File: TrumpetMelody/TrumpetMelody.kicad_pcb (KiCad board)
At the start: 2 copper layers, 76.2 x 68.6 mm, 79 parts, among them J1 USB_B_Micro, J2 Conn_01x05, J3 640456-3, J4 640456-3, SW1 SW_Push, U1 STM32F411RETx, U2 TLV62565DBVR, U3 MAX98357AETE_T, U4 MAX7375AXR805

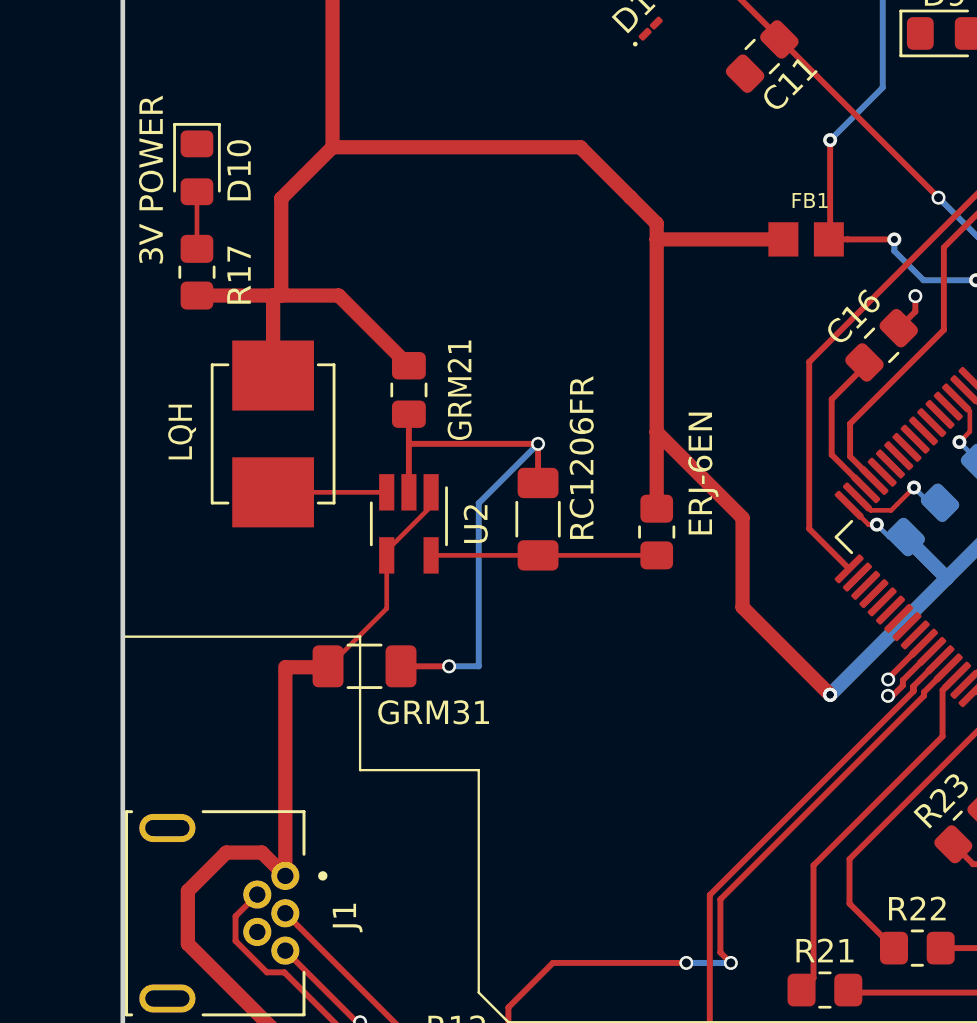
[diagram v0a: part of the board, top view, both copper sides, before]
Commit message: Manually added TI Webench PCB layout
I just sort of rotated the picture and drew it on
There's a bunch of holes in the PCB layout and I don't know if those are supposed to be vias or whatever. I may have used the wrong type of hole to switch board sides too.
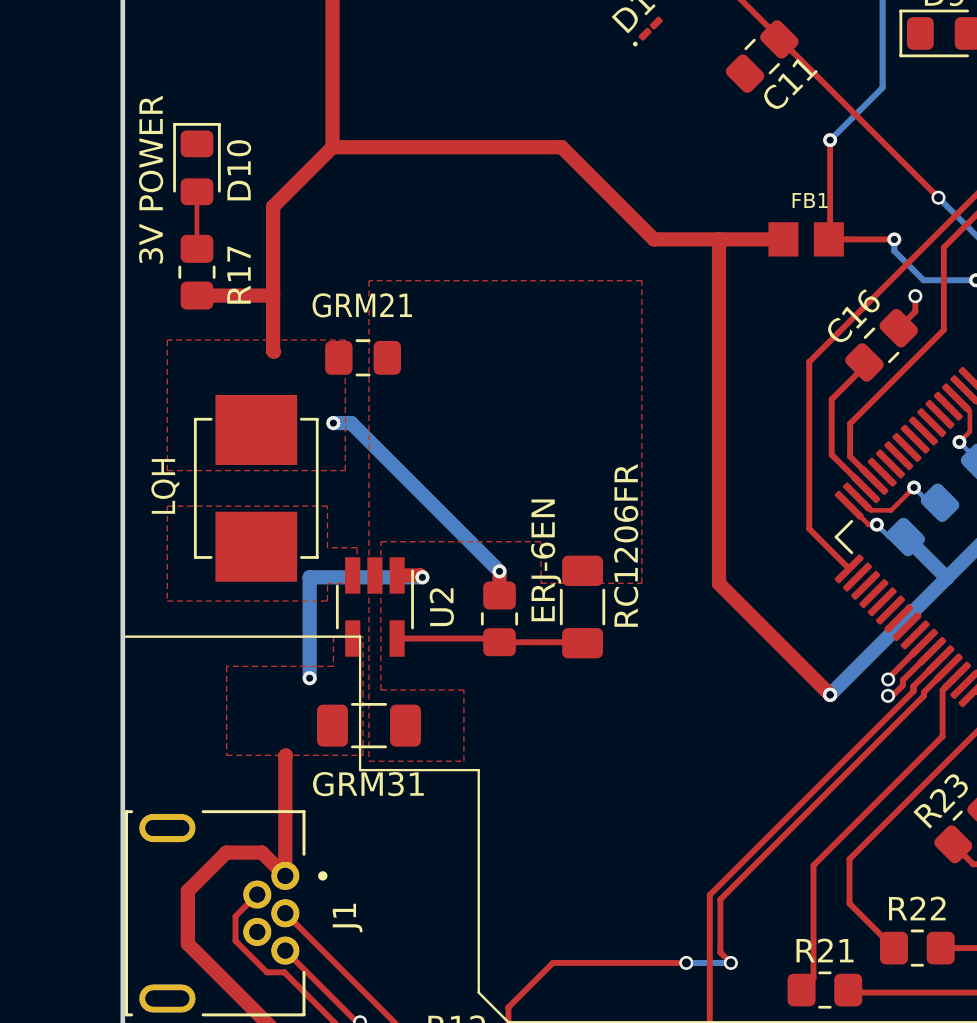
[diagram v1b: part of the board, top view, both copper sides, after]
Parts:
- moved ERJ-6EN 7.69 mm to (163.4, 86.9)
- moved RC1206FR 4.22 mm to (167.0, 86.4)
- moved U2 3.85 mm to (158.1, 86.4)
- moved GRM31 2.55 mm to (157.9, 91.4)
- moved LQH 2.44 mm to (153.0, 81.3)
- moved GRM21 2.40 mm to (157.6, 75.7), turned to 0 degrees
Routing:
- net GND: track 93.6 -> 69.2 mm, vias 15 -> 13
- net Net-(U2-SW): track 4.86 -> 0.00 mm
- net +5V: track 93.7 -> 89.0 mm, vias 0 -> 2
- net +3.3V: track 170.1 -> 168.2 mm, vias 9 -> 11
- net Net-(U2-FB): track 9.73 -> 8.02 mm
- added copper zone on F.Cu, net +3.3V
- added copper zone on F.Cu, net +5V
- added copper zone on F.Cu, net GND
- added copper zone on F.Cu, net Net-(U2-SW)

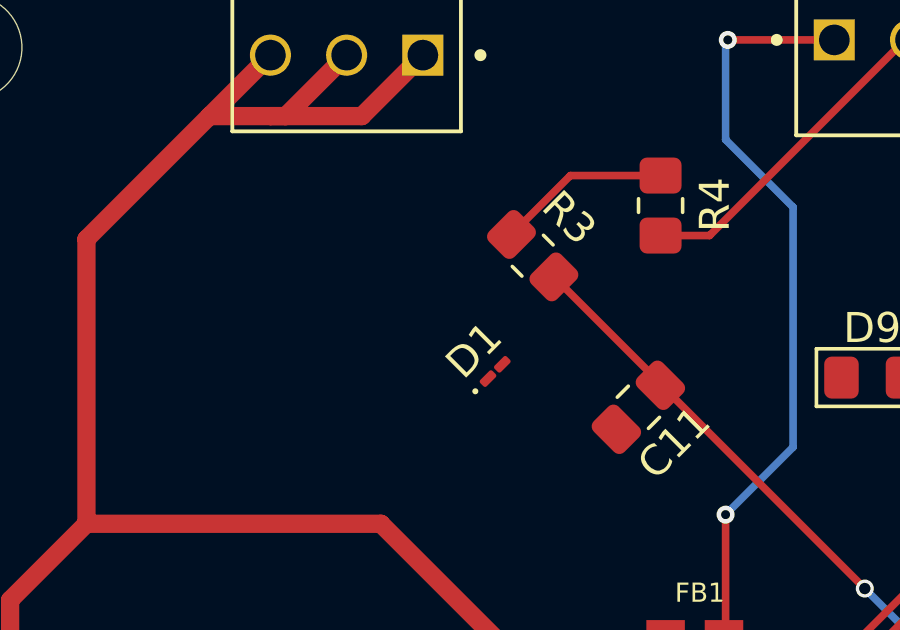
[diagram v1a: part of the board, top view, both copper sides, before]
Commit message: a diode on the linear pot got disconnected so i reconnected it
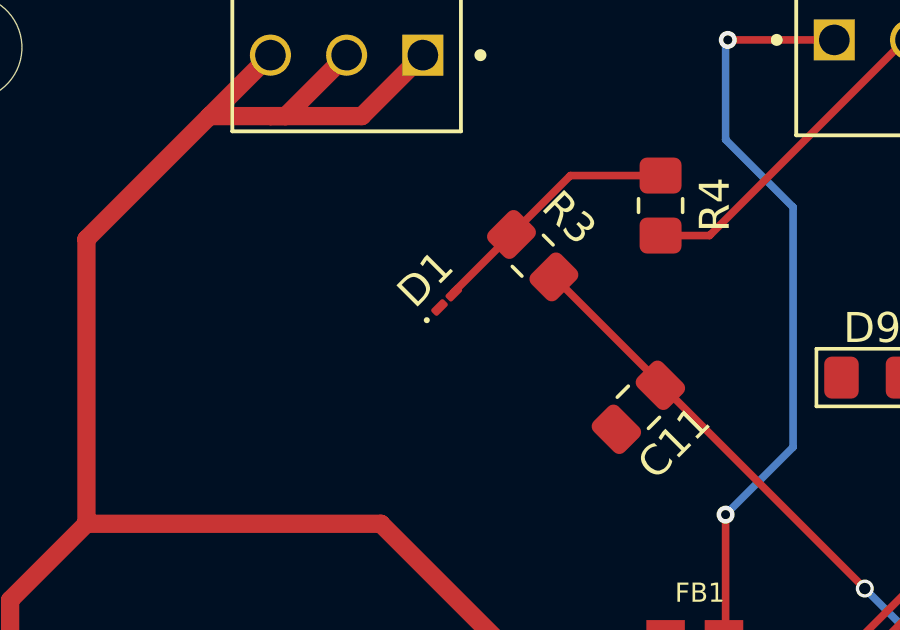
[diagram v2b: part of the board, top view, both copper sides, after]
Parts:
- moved D1 2.87 mm to (168.3, 59.2)
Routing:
- net Net-(D1-A2): track 5.78 -> 8.54 mm
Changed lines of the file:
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@@
   )
   (footprint "Diode_SMD:D_01005_0402Metric_Pad0.57x0.30mm_HandSolder" (layer "F.Cu")
-    (at 169.923674 61.597326 45)
+    (at 168.306325 59.227222 45)
     (descr "Diode SMD 01005 (0402 Metric), square (rectangular) end terminal, IPC_7351 nominal, (Body size source: http://www.vishay.com/docs/20056/crcw01005e3.pdf), generated with kicad-footprint-generator")
     (tags "diode handsolder")
@@
   (segment (start 194.937948 87.622948) (end 195.565896 86.995) (width 0.254) (layer "B.Cu") (net 13))
   (segment (start 210.185 69.85) (end 210.185 73.66) (width 0.254) (layer "B.Cu") (net 13))
+  (segment (start 168.544974 58.953798) (end 168.544974 58.988573) (width 0.254) (layer "F.Cu") (net 14))
   (segment (start 172.431572 55.0672) (end 175.4378 55.0672) (width 0.254) (layer "F.Cu") (net 14))
+  (segment (start 170.467586 57.031186) (end 168.544974 58.953798) (width 0.254) (layer "F.Cu") (net 14))
   (segment (start 170.467586 57.031186) (end 172.431572 55.0672) (width 0.254) (layer "F.Cu") (net 14))
   (segment (start 172.906777 98.880275) (end 172.906777 101.151777) (width 0.254) (layer "F.Cu") (net 15))

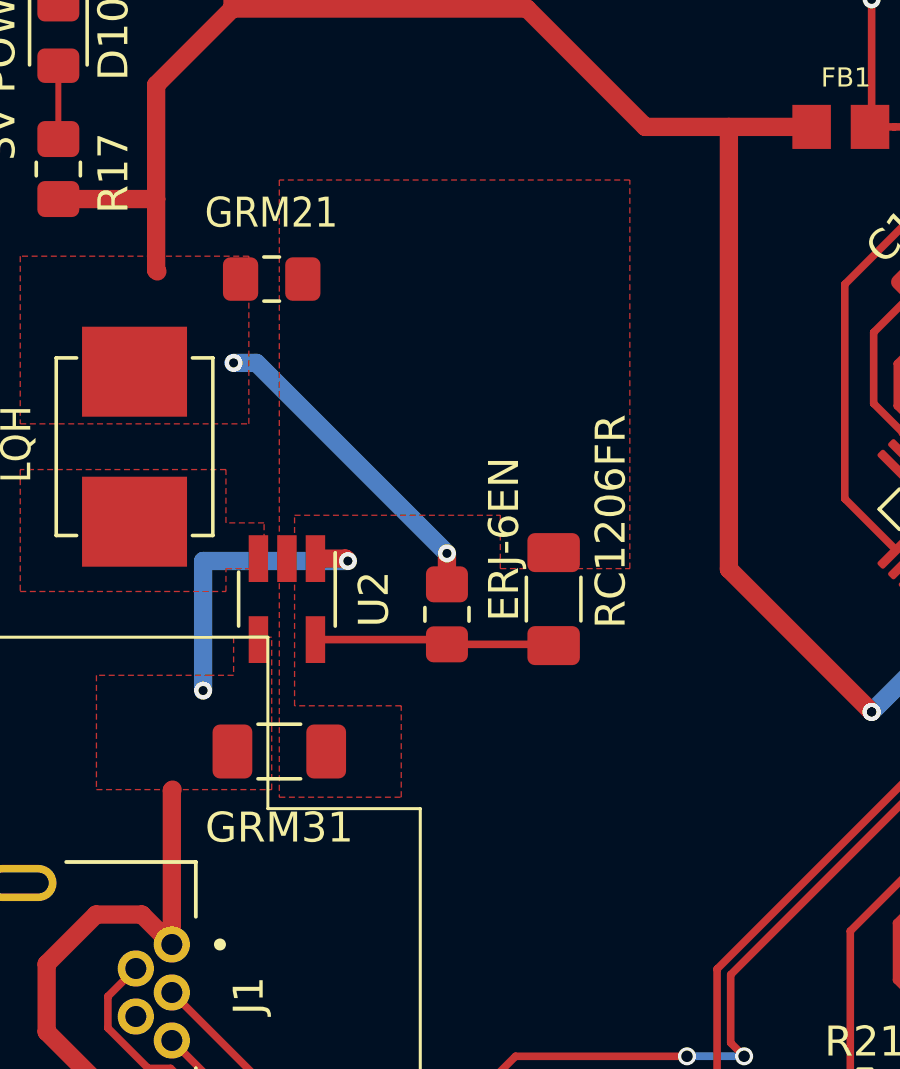
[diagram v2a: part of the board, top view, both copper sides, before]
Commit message: Added stitching vias
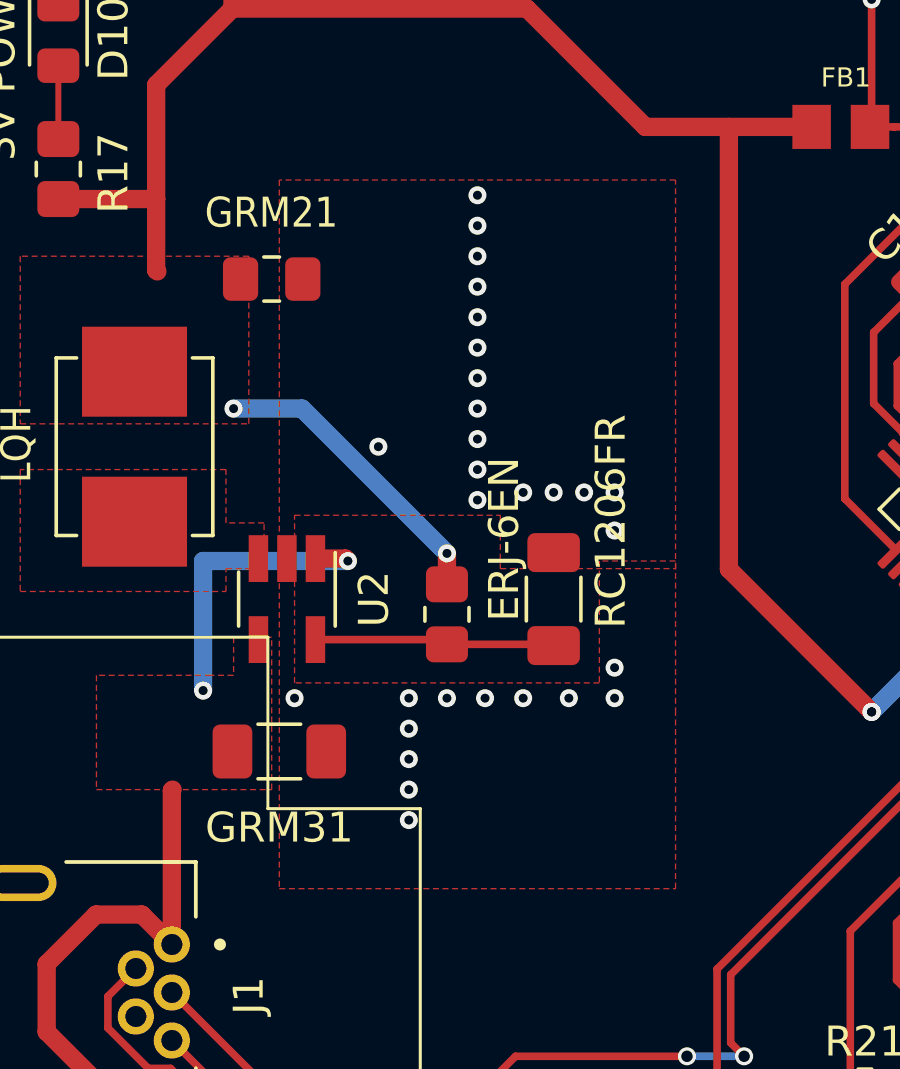
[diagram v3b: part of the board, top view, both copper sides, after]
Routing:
- net +3.3V: track 168.2 -> 167.5 mm
- net (no net): vias 0 -> 29
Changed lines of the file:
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@@
     (effects (font (size 1 1) (thickness 0.1)) (justify left bottom))
   )
+  (via (at 164.465 81.026) (size 0.6) (drill 0.3) (layers "F.Cu" "B.Cu") (net 0))
+  (via (at 168.021 82.804) (size 0.6) (drill 0.3) (layers "F.Cu" "B.Cu") (net 0))
+  (via (at 169.037 89.662) (size 0.6) (drill 0.3) (layers "F.Cu" "B.Cu") (net 0))
+  (via (at 162.179 89.662) (size 0.6) (drill 0.3) (layers "F.Cu" "B.Cu") (net 0))
+  (via (at 162.179 90.678) (size 0.6) (drill 0.3) (layers "F.Cu" "B.Cu") (net 0))
+  (via (at 161.163 81.28) (size 0.6) (drill 0.3) (layers "F.Cu" "B.Cu") (net 0))
+  (via (at 164.719 89.662) (size 0.6) (drill 0.3) (layers "F.Cu" "B.Cu") (net 0))
+  (via (at 164.465 78.994) (size 0.6) (drill 0.3) (layers "F.Cu" "B.Cu") (net 0))
+  (via (at 164.465 74.93) (size 0.6) (drill 0.3) (layers "F.Cu" "B.Cu") (net 0))
+  (via (at 164.465 80.01) (size 0.6) (drill 0.3) (layers "F.Cu" "B.Cu") (net 0))
+  (via (at 163.449 89.662) (size 0.6) (drill 0.3) (layers "F.Cu" "B.Cu") (net 0))
+  (via (at 165.989 89.662) (size 0.6) (drill 0.3) (layers "F.Cu" "B.Cu") (net 0))
+  (via (at 162.179 92.71) (size 0.6) (drill 0.3) (layers "F.Cu" "B.Cu") (net 0))
+  (via (at 164.465 75.946) (size 0.6) (drill 0.3) (layers "F.Cu" "B.Cu") (net 0))
+  (via (at 169.037 88.646) (size 0.6) (drill 0.3) (layers "F.Cu" "B.Cu") (net 0))
+  (via (at 162.179 93.726) (size 0.6) (drill 0.3) (layers "F.Cu" "B.Cu") (net 0))
+  (via (at 164.465 82.042) (size 0.6) (drill 0.3) (layers "F.Cu" "B.Cu") (net 0))
+  (via (at 164.465 73.914) (size 0.6) (drill 0.3) (layers "F.Cu" "B.Cu") (net 0))
+  (via (at 162.179 91.694) (size 0.6) (drill 0.3) (layers "F.Cu" "B.Cu") (net 0))
+  (via (at 164.465 83.058) (size 0.6) (drill 0.3) (layers "F.Cu" "B.Cu") (net 0))
+  (via (at 165.989 82.804) (size 0.6) (drill 0.3) (layers "F.Cu" "B.Cu") (net 0))
+  (via (at 158.369 89.662) (size 0.6) (drill 0.3) (layers "F.Cu" "B.Cu") (net 0))
+  (via (at 167.005 82.804) (size 0.6) (drill 0.3) (layers "F.Cu" "B.Cu") (net 0))
+  (via (at 169.037 84.074) (size 0.6) (drill 0.3) (layers "F.Cu" "B.Cu") (net 0))
+  (via (at 164.465 76.962) (size 0.6) (drill 0.3) (layers "F.Cu" "B.Cu") (net 0))
+  (via (at 169.037 82.804) (size 0.6) (drill 0.3) (layers "F.Cu" "B.Cu") (net 0))
+  (via (at 167.513 89.662) (size 0.6) (drill 0.3) (layers "F.Cu" "B.Cu") (net 0))
+  (via (at 164.465 77.978) (size 0.6) (drill 0.3) (layers "F.Cu" "B.Cu") (net 0))
+  (via (at 164.465 72.898) (size 0.6) (drill 0.3) (layers "F.Cu" "B.Cu") (net 0))
   (segment (start 170.061 70.62) (end 175.605 70.62) (width 0.61) (layer "F.Cu") (net 1))
   (segment (start 156.3 57.187) (end 160.401 53.086) (width 0.61) (layer "F.Cu") (net 1))
@@
   (via (at 187.560857 86.900017) (size 0.6) (drill 0.3) (layers "F.Cu" "B.Cu") (net 1))
   (via (at 190.566061 83.894813) (size 0.6) (drill 0.3) (layers "F.Cu" "B.Cu") (net 1))
-  (via (at 156.337 78.486) (size 0.6) (drill 0.3) (layers "F.Cu" "B.Cu") (net 1))
+  (via (at 156.337 80.01) (size 0.6) (drill 0.3) (layers "F.Cu" "B.Cu") (net 1))
   (via (at 190.742837 83.01093) (size 0.6) (drill 0.3) (layers "F.Cu" "B.Cu") (net 1))
   (via (at 179.605905 82.834153) (size 0.6) (drill 0.3) (layers "F.Cu" "B.Cu") (net 1))
@@
   (segment (start 185.855 81.87) (end 185.71282 81.87) (width 0.61) (layer "B.Cu") (net 1))
   (segment (start 177.605 90.12) (end 182.605 85.12) (width 0.61) (layer "B.Cu") (net 1))
-  (segment (start 163.449 84.836) (end 157.099 78.486) (width 0.61) (layer "B.Cu") (net 1))
   (segment (start 184.23 83.495) (end 184.23 83.816648) (width 0.61) (layer "B.Cu") (net 1))
   (segment (start 193.415 83.56) (end 192.79 82.935) (width 0.61) (layer "B.Cu") (net 1))
@@
   (segment (start 182.605 85.12) (end 182.59886 85.12) (width 0.61) (layer "B.Cu") (net 1))
   (segment (start 179.605905 82.834153) (end 180.136236 83.364483) (width 0.2) (layer "B.Cu") (net 1))
+  (segment (start 158.623 80.01) (end 163.449 84.836) (width 0.61) (layer "B.Cu") (net 1))
   (segment (start 186.355 81.37) (end 188.041246 81.37) (width 0.61) (layer "B.Cu") (net 1))
   (segment (start 193.855 83.12) (end 194.355 83.12) (width 0.3) (layer "B.Cu") (net 1))
@@
   (segment (start 187.560857 86.900017) (end 186.447164 85.786324) (width 0.2) (layer "B.Cu") (net 1))
   (segment (start 193.415 83.56) (end 193.855 83.12) (width 0.3) (layer "B.Cu") (net 1))
-  (segment (start 157.099 78.486) (end 156.337 78.486) (width 0.61) (layer "B.Cu") (net 1))
   (segment (start 198.501 84.074) (end 193.929 84.074) (width 0.61) (layer "B.Cu") (net 1))
+  (segment (start 156.337 80.01) (end 158.623 80.01) (width 0.61) (layer "B.Cu") (net 1))
   (segment (start 182.59886 85.12) (end 180.843343 83.364483) (width 0.61) (layer "B.Cu") (net 1))
   (segment (start 184.23 83.816648) (end 186.199676 85.786324) (width 0.61) (layer "B.Cu") (net 1))
@@
     (connect_pads (clearance 0.5))
     (min_thickness 0.25) (filled_areas_thickness no)
-    (fill yes (thermal_gap 0.5) (thermal_bridge_width 0.5))
+    (fill (thermal_gap 0.5) (thermal_bridge_width 0.5))
     (polygon
       (pts
@@
     (connect_pads (clearance 0.5))
     (min_thickness 0.25) (filled_areas_thickness no)
-    (fill yes (thermal_gap 0.5) (thermal_bridge_width 0.5))
+    (fill (thermal_gap 0.5) (thermal_bridge_width 0.5))
     (polygon
       (pts
@@
     (connect_pads (clearance 0.5))
     (min_thickness 0.25) (filled_areas_thickness no)
-    (fill yes (thermal_gap 0.5) (thermal_bridge_width 0.5))
+    (fill (thermal_gap 0.5) (thermal_bridge_width 0.5))
     (polygon
       (pts
         (xy 157.861 72.39)
-        (xy 157.861 92.964)
-        (xy 161.925 92.964)
-        (xy 161.925 89.916)
-        (xy 158.369 89.916)
+        (xy 157.861 96.012)
+        (xy 171.069 96.012)
+        (xy 171.069 90.17)
+        (xy 171.069 85.09)
+        (xy 168.529 85.09)
+        (xy 168.529 89.154)
+        (xy 158.369 89.154)
         (xy 158.369 83.566)
         (xy 165.227 83.566)
         (xy 165.227 85.344)
-        (xy 169.545 85.344)
-        (xy 169.545 72.39)
+        (xy 171.069 85.344)
+        (xy 171.069 72.39)
       )
     )
@@
     (connect_pads (clearance 0.5))
     (min_thickness 0.25) (filled_areas_thickness no)
-    (fill yes (thermal_gap 0.5) (thermal_bridge_width 0.5))
+    (fill (thermal_gap 0.5) (thermal_bridge_width 0.5))
     (polygon
       (pts
